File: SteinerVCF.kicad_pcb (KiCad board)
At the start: 2 copper layers, 56 parts, among them J5 Conn_02x05_Odd_Even, Q1 BC847, Q2 BC847, U1 TL074

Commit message: Early placement.
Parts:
- added C15: 100n, Capacitor_SMD:C_0603_1608Metric, B.Cu at (195.1, 135.4)
- added C16: 100n, Capacitor_SMD:C_0603_1608Metric, B.Cu at (195.1, 133.9)
- added C17: 100n, Capacitor_SMD:C_0603_1608Metric, B.Cu at (195.1, 136.9)
- added C18: 100n, Capacitor_SMD:C_0603_1608Metric, B.Cu at (180.6, 120.2)
- added J1: AudioJack2_Ground_Switch, Local:PJ398SM, F.Cu at (58.4, 68.6)
- added J2: AudioJack2_Ground_Switch, Local:PJ398SM, F.Cu at (58.4, 81.3)
- added J3: AudioJack2_Ground_Switch, Local:PJ398SM, F.Cu at (58.4, 94.0)
- added J4: AudioJack2_Ground_Switch, Local:PJ398SM, F.Cu at (58.4, 106.7)
- added J6: AudioJack2_Ground_Switch, Local:PJ398SM, F.Cu at (58.4, 119.4)
- added R25: 4k7, Resistor_SMD:R_0603_1608Metric, B.Cu at (116.2, 110.5)
- added R26: 1M, Resistor_SMD:R_0603_1608Metric, B.Cu at (104.8, 110.5)
- added R27: 3k9, Resistor_SMD:R_0603_1608Metric, B.Cu at (131.4, 110.5)
- added R28: 220k, Resistor_SMD:R_0603_1608Metric, B.Cu at (102.2, 110.5)
- added R29: 10k, Resistor_SMD:R_0603_1608Metric, B.Cu at (102.2, 87.0)
- added R30: 22k, Resistor_SMD:R_0603_1608Metric, B.Cu at (99.7, 110.5)
- added R31: 220k, Resistor_SMD:R_0603_1608Metric, B.Cu at (104.8, 87.0)
- added R32: 1k, Resistor_SMD:R_0603_1608Metric, B.Cu at (99.7, 87.0)
- added RV1: 100k, Local:AlpsRK09K, F.Cu at (58.4, 33.0)
- added RV2: 1k, Potentiometer_THT:Potentiometer_Bourns_3296W_Vertical, B.Cu at (183.7, 129.2)
- added RV3: 100k, Local:AlpsRK09K, F.Cu at (58.4, 53.3)
- added U2: TL072, Package_SO:SOIC-8_3.9x4.9mm_P1.27mm, B.Cu at (110.5, 85.1)
- added U3: TL072, Package_SO:SOIC-8_3.9x4.9mm_P1.27mm, B.Cu at (110.5, 110.5)
- C1, C10, C11, C12, C13, C14, C2, C4, C6, C7, C8, C9, D1, D10, D11, D12, D13, D14, D2, D3, D4, D7, J5, Q1, Q2: moved to B.Cu
- C3: value 2.2u -> 10u; footprint Capacitor_SMD:CP_Elec_4x5.4 -> Capacitor_SMD:CP_Elec_4x5.8; moved to B.Cu
- C5: value 10u -> 2.2u; footprint Capacitor_SMD:CP_Elec_4x5.8 -> Capacitor_SMD:CP_Elec_4x5.4; moved to B.Cu
- D5, D6: value 1N4148W -> DFLR1400-7; footprint Diode_SMD:D_SOD-123 -> Diode_SMD:D_PowerDI-123; moved to B.Cu
- D8, D9: value DFLR1400-7 -> 1N4148W; footprint Diode_SMD:D_PowerDI-123 -> Diode_SMD:D_SOD-123; moved to B.Cu
- R1, R2, R3: value 47k -> 100k; moved to B.Cu
- R10: value 390 -> 47k; moved to B.Cu
- R11: value 1k -> 47k; moved to B.Cu
- R12: value 1k -> 220k; moved to B.Cu
- R13: value 1k8 -> 180k; moved to B.Cu
- R14: value 1k -> 180k; moved to B.Cu
- R15: value 2200k -> 1k8; moved to B.Cu
- R16: value 22k -> 3k9; moved to B.Cu
- R17: value 4k7 -> 82; moved to B.Cu
- R18: value 1M -> 390; moved to B.Cu
- R19: value 3k9 -> 1k; moved to B.Cu
- R20: value 220k -> 1k; moved to B.Cu
- R21: value 10k -> 1k8; moved to B.Cu
- R22: value 22k -> 1k; moved to B.Cu
- R23: value 220k -> 2200k; moved to B.Cu
- R24: value 1k -> 22k; moved to B.Cu
- R4: value 220k -> 100k; moved to B.Cu
- R5, R6: value 180k -> 100k; moved to B.Cu
- R7: value 1k8 -> 100k; moved to B.Cu
- R8: value 3k9 -> 150k; moved to B.Cu
- R9: value 82 -> 47k; moved to B.Cu
- U1: value TL074 -> TL072; footprint Package_SO:SOIC-14_3.9x8.7mm_P1.27mm -> Package_SO:SOIC-8_3.9x4.9mm_P1.27mm; moved to B.Cu
- moved D5 91.5 mm to (81.9, 35.6)
- moved C3 88.6 mm to (82.5, 29.2)
- moved C4 87.6 mm to (92.7, 29.2)
- moved D6 85.0 mm to (93.3, 34.9)
- moved J5 76.2 mm to (63.5, 38.1)
- moved R16 67.2 mm to (183.8, 62.6)
- moved R14 67.2 mm to (180.8, 62.6)
- moved R22 67.2 mm to (186.8, 62.6)
- moved D2 66.9 mm to (176.9, 62.8)
- moved D8 66.3 mm to (162.5, 63.3)
- moved R4 65.0 mm to (182.7, 64.2)
- moved R15 65.0 mm to (185.7, 64.2)
- moved R19 63.7 mm to (188.7, 65.0)
- moved R8 62.8 mm to (185.7, 65.7)
- moved C1 62.0 mm to (196.6, 72.0)
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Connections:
- C1 pad 2: GND -> (no net)
- C10 pad 2: GND -> (no net)
- C2 pad 1: GND -> (no net)
- C3 pad 1: Net-(C11-Pad2) -> +12V
- C3 pad 2: Net-(C3-Pad2) -> (no net)
- C4 pad 1: +12V -> (no net)
- C4 pad 2: GND -> -12V
- C5 pad 1: GND -> Net-(C11-Pad2)
- C5 pad 2: -12V -> Net-(C5-Pad2)
- C9 pad 1: GND -> (no net)
- D5 pad 1: Net-(D4-Pad2) -> +12V
- D5 pad 2: Net-(C12-Pad2) -> Net-(D5-Pad2)
- D6 pad 1: Net-(C12-Pad2) -> Net-(D6-Pad1)
- D6 pad 2: Net-(D6-Pad2) -> -12V
- D7 pad 1: Net-(D6-Pad2) -> Net-(D4-Pad2)
- D7 pad 2: Net-(C11-Pad1) -> Net-(C12-Pad2)
- D8 pad 1: +12V -> Net-(C12-Pad2)
- D9 pad 1: Net-(D9-Pad1) -> Net-(D8-Pad2)
- D9 pad 2: -12V -> Net-(C11-Pad1)
- J5 pad 1: Net-(D9-Pad1) -> Net-(D6-Pad1)
- J5 pad 10: Net-(D8-Pad2) -> Net-(D5-Pad2)
- J5 pad 2: Net-(D9-Pad1) -> Net-(D6-Pad1)
- J5 pad 3: GND -> (no net)
- J5 pad 4: GND -> (no net)
- J5 pad 5: GND -> (no net)
- J5 pad 6: GND -> (no net)
- J5 pad 7: GND -> (no net)
- J5 pad 8: GND -> (no net)
- J5 pad 9: Net-(D8-Pad2) -> Net-(D5-Pad2)
- Q2 pad 1: GND -> (no net)
- R1 pad 1: Net-(C6-Pad2) -> Net-(R1-Pad1)
- R10 pad 1: +12V -> Net-(C8-Pad2)
- R10 pad 2: Net-(C10-Pad1) -> Net-(R10-Pad2)
- R11 pad 1: Net-(C6-Pad1) -> Net-(C5-Pad2)
- R11 pad 2: Net-(C10-Pad1) -> Net-(R11-Pad2)
- R12 pad 1: Net-(C8-Pad2) -> Net-(J4-PadT)
- R12 pad 2: GND -> Net-(Q1-Pad1)
- R13 pad 1: Net-(R13-Pad1) -> Net-(C6-Pad2)
- R13 pad 2: Net-(D12-Pad2) -> (no net)
- R14 pad 1: Net-(R14-Pad1) -> Net-(C5-Pad2)
- R14 pad 2: Net-(C11-Pad2) -> (no net)
- R15 pad 1: Net-(C12-Pad1) -> Net-(R15-Pad1)
- R15 pad 2: GND -> Net-(D1-Pad1)
- R16 pad 1: Net-(D13-Pad1) -> Net-(Q1-Pad2)
- R16 pad 2: GND -> Net-(C9-Pad2)
- R17 pad 1: Net-(C13-Pad1) -> Net-(C9-Pad2)
- R17 pad 2: Net-(D13-Pad1) -> -12V
- R18 pad 1: Net-(R18-Pad1) -> +12V
- R18 pad 2: GND -> Net-(C10-Pad1)
- R19 pad 1: Net-(C13-Pad1) -> Net-(C6-Pad1)
- R19 pad 2: Net-(R19-Pad2) -> Net-(C10-Pad1)
- R2 pad 1: Net-(C8-Pad2) -> Net-(R2-Pad1)
- R20 pad 1: Net-(C14-Pad1) -> Net-(C8-Pad2)
- R20 pad 2: Net-(R18-Pad1) -> (no net)
- R21 pad 2: Net-(C13-Pad2) -> Net-(D12-Pad2)
- R22 pad 1: Net-(R19-Pad2) -> Net-(R22-Pad1)
- R22 pad 2: Net-(C14-Pad2) -> Net-(C11-Pad2)
- R23 pad 1: Net-(R23-Pad1) -> Net-(C12-Pad1)
- R23 pad 2: Net-(R21-Pad1) -> (no net)
- R24 pad 1: Net-(J6-PadT) -> Net-(D13-Pad1)
- R24 pad 2: Net-(R23-Pad1) -> (no net)
- R3 pad 1: Net-(C3-Pad2) -> Net-(R3-Pad1)
- R4 pad 2: Net-(Q1-Pad1) -> +12V
- R5 pad 1: Net-(C6-Pad2) -> Net-(R5-Pad1)
- R5 pad 2: GND -> Net-(R1-Pad1)
- R6 pad 1: Net-(C3-Pad2) -> Net-(R10-Pad2)
- R6 pad 2: GND -> Net-(R2-Pad1)
- R7 pad 1: Net-(R7-Pad1) -> Net-(R11-Pad2)
- R7 pad 2: Net-(D1-Pad1) -> Net-(R3-Pad1)
- R8 pad 1: Net-(Q1-Pad2) -> Net-(Q1-Pad1)
- R8 pad 2: Net-(C9-Pad2) -> Net-(R8-Pad2)
- R9 pad 1: Net-(C9-Pad2) -> Net-(C6-Pad2)
- R9 pad 2: -12V -> Net-(R5-Pad1)
- U1 pad 1: Net-(U1-Pad1) -> Net-(R10-Pad2)
- U1 pad 2: Net-(U1-Pad2) -> Net-(R2-Pad1)
- U1 pad 3: Net-(U1-Pad3) -> (no net)
- U1 pad 4: +12V -> -12V
- U1 pad 5: Net-(R18-Pad1) -> (no net)
- U1 pad 6: Net-(R14-Pad1) -> Net-(R1-Pad1)
- U1 pad 7: Net-(R14-Pad1) -> Net-(R5-Pad1)
- U1 pad 8: Net-(C13-Pad1) -> +12V

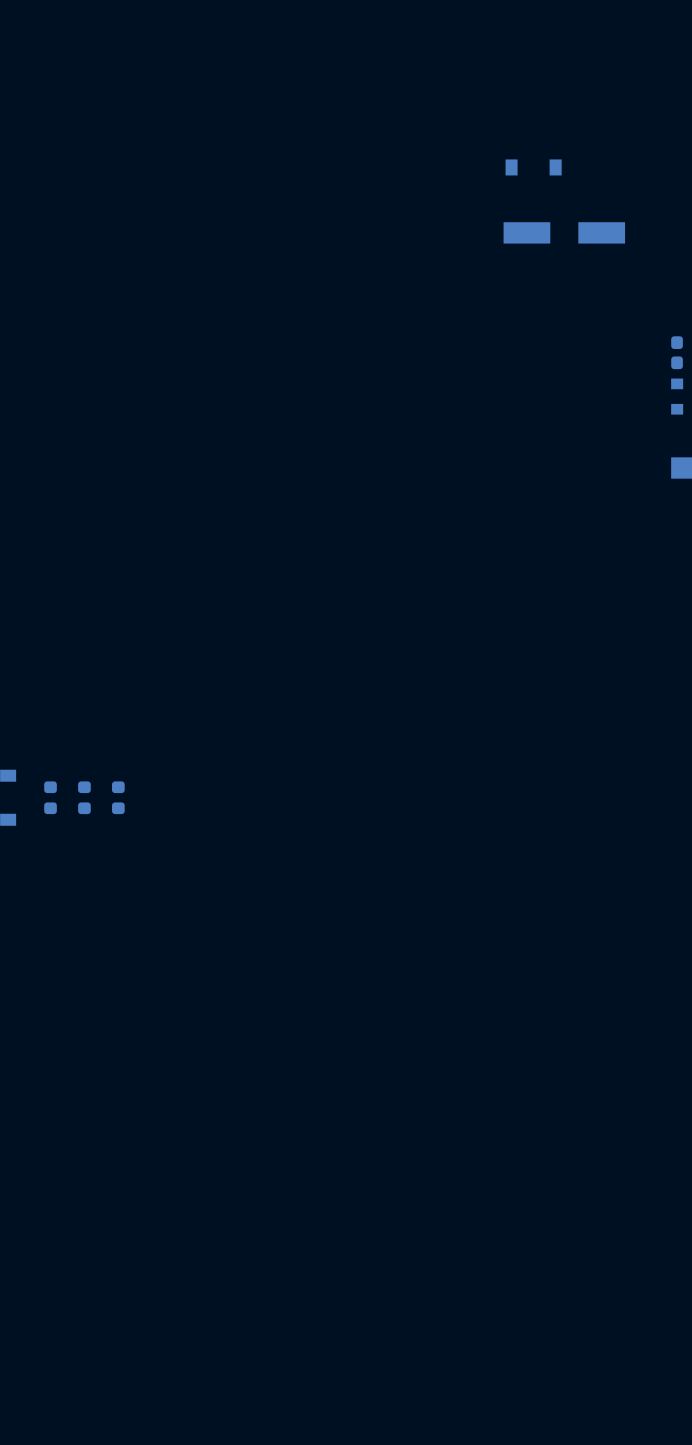
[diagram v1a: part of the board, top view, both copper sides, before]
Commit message: Added edge-cuts.
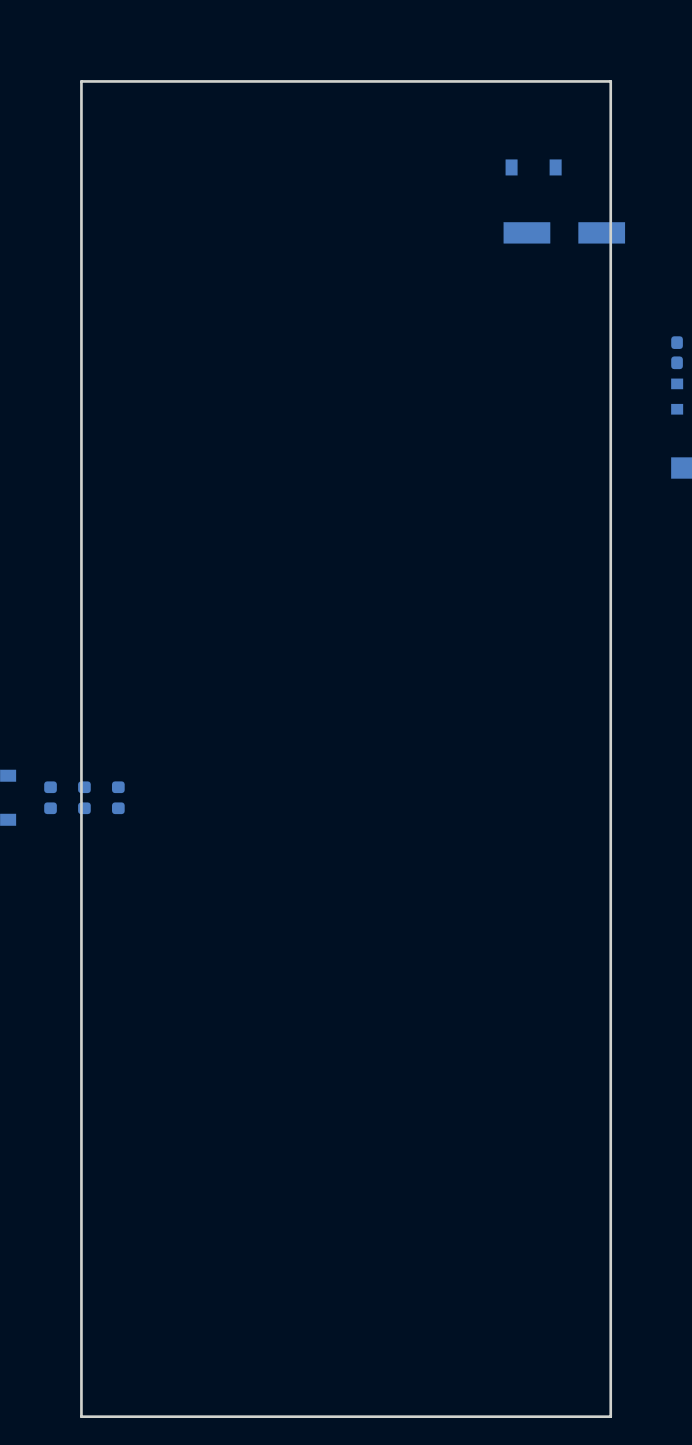
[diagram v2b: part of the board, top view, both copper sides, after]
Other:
- board outline added: 39.6 x 100 mm
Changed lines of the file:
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@@
   (general
     (thickness 1.6)
-    (drawings 5)
+    (drawings 58)
     (tracks 0)
     (zones 0)
@@
     )
   )
-  (gr_line (start 68.58508 24.765) (end 68.58 124.76226) (layer Dwgs.User) (width 0.2))
-  (gr_line (start 48.26 122.85726) (end 48.26762 122.85726) (layer Dwgs.User) (width 0.2))
-  (gr_line (start 48.25746 24.76246) (end 48.26 124.76226) (layer Dwgs.User) (width 0.2))
-  (gr_line (start 48.26 124.765) (end 68.58 124.765) (layer Dwgs.User) (width 0.2))
-  (gr_line (start 48.26 24.765) (end 68.58 24.765) (layer Dwgs.User) (width 0.2))
+  (gr_line (start 128.6811 56.843234) (end 128.6811 156.843234) (layer Edge.Cuts) (width 0.2))
+  (gr_line (start 168.3211 156.843234) (end 168.3211 56.843234) (layer Edge.Cuts) (width 0.2))
+  (gr_line (start 128.6811 156.843234) (end 168.3211 156.843234) (layer Edge.Cuts) (width 0.2))
+  (gr_line (start 168.3211 56.843234) (end 128.6811 56.843234) (layer Edge.Cuts) (width 0.2))
+  (gr_circle (center 137.1811 166.2536) (end 138.6811 166.2536) (layer Dwgs.User) (width 0.2))
+  (gr_circle (center 162.5811 166.2536) (end 164.0811 166.2536) (layer Dwgs.User) (width 0.2))
+  (gr_circle (center 161.0811 43.7536) (end 162.5811 43.7536) (layer Dwgs.User) (width 0.2))
+  (gr_circle (center 158.6611 150.7236) (end 161.6611 150.7236) (layer Dwgs.User) (width 0.2))
+  (gr_circle (center 135.6811 43.7536) (end 137.1811 43.7536) (layer Dwgs.User) (width 0.2))
+  (gr_line (start 162.5811 42.2536) (end 159.5811 42.2536) (layer Dwgs.User) (width 0.2))
+  (gr_line (start 168.3211 51.7536) (end 128.6811 51.7536) (layer Dwgs.User) (width 0.2))
+  (gr_line (start 128.6811 51.7536) (end 128.6811 158.2536) (layer Dwgs.User) (width 0.2))
+  (gr_line (start 128.1811 169.2536) (end 168.8211 169.2536) (layer Dwgs.User) (width 0.2))
+  (gr_line (start 162.5811 43.7536) (end 159.5811 43.7536) (layer Dwgs.User) (width 0.2))
+  (gr_circle (center 159.5811 166.2536) (end 161.0811 166.2536) (layer Dwgs.User) (width 0.2))
+  (gr_line (start 137.1811 42.2536) (end 134.1811 42.2536) (layer Dwgs.User) (width 0.2))
+  (gr_line (start 168.8211 40.7536) (end 128.1811 40.7536) (layer Dwgs.User) (width 0.2))
+  (gr_line (start 128.6811 55.0036) (end 168.3211 55.0036) (layer Dwgs.User) (width 0.2))
+  (gr_circle (center 138.3411 64.3636) (end 141.8411 64.3636) (layer Dwgs.User) (width 0.2))
+  (gr_circle (center 138.3411 150.7236) (end 141.3411 150.7236) (layer Dwgs.User) (width 0.2))
+  (gr_circle (center 138.3411 105.0036) (end 141.3411 105.0036) (layer Dwgs.User) (width 0.2))
+  (gr_circle (center 135.6811 166.2536) (end 137.1811 166.2536) (layer Dwgs.User) (width 0.2))
+  (gr_line (start 120.5611 155.8036) (end 125.6411 155.8036) (layer Dwgs.User) (width 0.2))
+  (gr_line (start 159.5811 167.7536) (end 162.5811 167.7536) (layer Dwgs.User) (width 0.2))
+  (gr_line (start 159.5811 45.2536) (end 162.5811 45.2536) (layer Dwgs.User) (width 0.2))
+  (gr_line (start 137.1811 43.7536) (end 134.1811 43.7536) (layer Dwgs.User) (width 0.2))
+  (gr_line (start 134.1811 167.7536) (end 137.1811 167.7536) (layer Dwgs.User) (width 0.2))
+  (gr_circle (center 138.3411 120.2436) (end 141.3411 120.2436) (layer Dwgs.User) (width 0.2))
+  (gr_circle (center 158.6611 120.2436) (end 161.6611 120.2436) (layer Dwgs.User) (width 0.2))
+  (gr_line (start 168.5711 105.0036) (end 128.6811 105.0036) (layer Dwgs.User) (width 0.2))
+  (gr_line (start 137.1811 166.2536) (end 134.1811 166.2536) (layer Dwgs.User) (width 0.2))
+  (gr_line (start 168.5711 40.7536) (end 128.4311 40.7536) (layer Dwgs.User) (width 0.2))
+  (gr_circle (center 159.5811 43.7536) (end 161.0811 43.7536) (layer Dwgs.User) (width 0.2))
+  (gr_line (start 128.4311 40.7536) (end 128.4311 169.2536) (layer Dwgs.User) (width 0.2))
+  (gr_circle (center 158.6611 135.4836) (end 161.6611 135.4836) (layer Dwgs.User) (width 0.2))
+  (gr_circle (center 161.0811 166.2536) (end 162.5811 166.2536) (layer Dwgs.User) (width 0.2))
+  (gr_circle (center 134.1811 43.7536) (end 135.6811 43.7536) (layer Dwgs.User) (width 0.2))
+  (gr_line (start 162.5811 166.2536) (end 159.5811 166.2536) (layer Dwgs.User) (width 0.2))
+  (gr_circle (center 137.1811 43.7536) (end 138.6811 43.7536) (layer Dwgs.User) (width 0.2))
+  (gr_line (start 162.5811 164.7536) (end 159.5811 164.7536) (layer Dwgs.User) (width 0.2))
+  (gr_line (start 148.5011 40.7536) (end 148.5011 169.2536) (layer Dwgs.User) (width 0.2))
+  (gr_circle (center 158.6611 105.0036) (end 161.6611 105.0036) (layer Dwgs.User) (width 0.2))
+  (gr_line (start 128.4311 169.2536) (end 168.5711 169.2536) (layer Dwgs.User) (width 0.2))
+  (gr_line (start 123.1011 153.2636) (end 123.1011 158.3436) (layer Dwgs.User) (width 0.2))
+  (gr_circle (center 158.6611 64.3636) (end 162.1611 64.3636) (layer Dwgs.User) (width 0.2))
+  (gr_line (start 168.5711 169.2536) (end 168.5711 40.7536) (layer Dwgs.User) (width 0.2))
+  (gr_circle (center 158.6611 84.6836) (end 162.1611 84.6836) (layer Dwgs.User) (width 0.2))
+  (gr_circle (center 138.3411 84.6836) (end 141.8411 84.6836) (layer Dwgs.User) (width 0.2))
+  (gr_line (start 128.6811 155.0036) (end 168.3211 155.0036) (layer Dwgs.User) (width 0.2))
+  (gr_circle (center 134.1811 166.2536) (end 135.6811 166.2536) (layer Dwgs.User) (width 0.2))
+  (gr_circle (center 138.3411 135.4836) (end 141.3411 135.4836) (layer Dwgs.User) (width 0.2))
+  (gr_line (start 134.1811 45.2536) (end 137.1811 45.2536) (layer Dwgs.User) (width 0.2))
+  (gr_line (start 128.1811 40.7536) (end 128.1811 169.2536) (layer Dwgs.User) (width 0.2))
+  (gr_line (start 168.8211 169.2536) (end 168.8211 40.7536) (layer Dwgs.User) (width 0.2))
+  (gr_line (start 168.3211 158.2536) (end 168.3211 51.7536) (layer Dwgs.User) (width 0.2))
+  (gr_circle (center 162.5811 43.7536) (end 164.0811 43.7536) (layer Dwgs.User) (width 0.2))
+  (gr_line (start 128.6811 158.2536) (end 168.3211 158.2536) (layer Dwgs.User) (width 0.2))
+  (gr_line (start 137.1811 164.7536) (end 134.1811 164.7536) (layer Dwgs.User) (width 0.2))
 )
